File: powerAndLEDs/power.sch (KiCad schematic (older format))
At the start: 23 parts, among them J1 Conn_Coaxial_Power, J2 GS3, J3 Screw_Terminal_01x02, SW1 SW_SPST

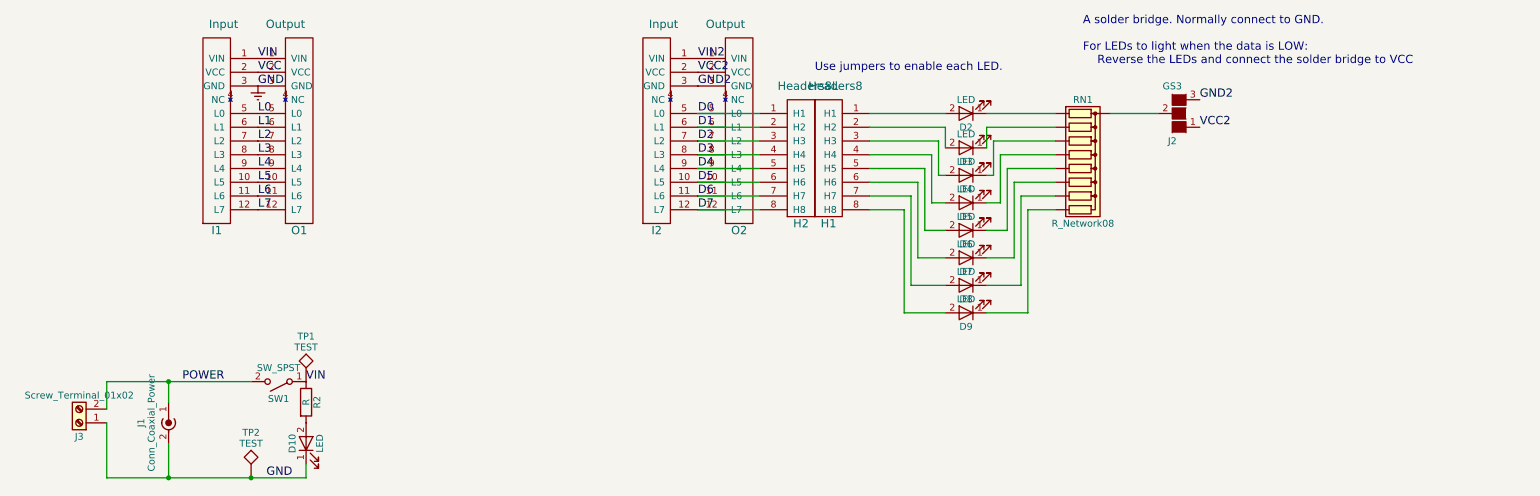
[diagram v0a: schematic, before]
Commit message: More update to make the libraryies use only relative paths.
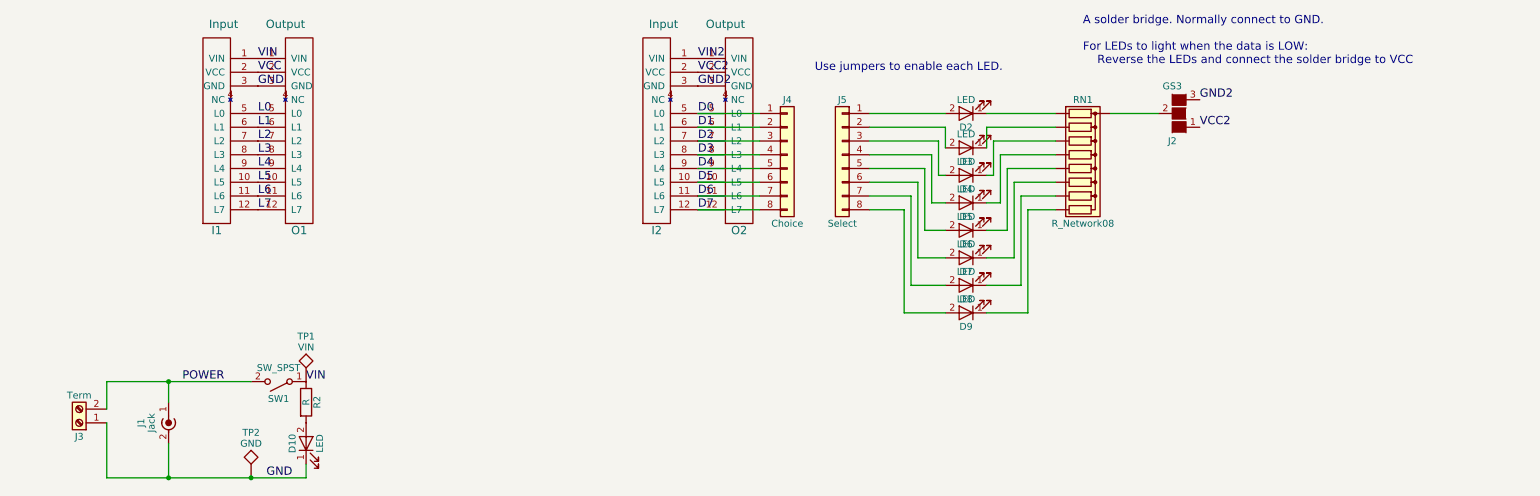
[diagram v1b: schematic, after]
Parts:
- removed H1: Headers8, Pin_Headers:Pin_Header_Straight_1x08_Pitch2.54mm, symbol Headers8
- removed H2: Headers8L, Pin_Headers:Pin_Header_Straight_1x08_Pitch2.54mm, symbol Headers8L
- added J4: Choice, Pin_Headers:Pin_Header_Straight_1x08_Pitch2.54mm, symbol Conn_01x08
- added J5: Select, Pin_Headers:Pin_Header_Straight_1x08_Pitch2.54mm, symbol Conn_01x08
- J1: value Conn_Coaxial_Power -> Jack
- J3: value Screw_Terminal_01x02 -> Term
- TP1: value TEST -> VIN
- TP2: value TEST -> GND
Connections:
- net D0: now also J4.1 (Pin_1)
- net D1: now also J4.2 (Pin_2)
- net D2: now also J4.3 (Pin_3)
- net D3: now also J4.4 (Pin_4)
- net D4: now also J4.5 (Pin_5)
- net D5: now also J4.6 (Pin_6)
- net D6: now also J4.7 (Pin_7)
- net D7: now also J4.8 (Pin_8)
- net at D2.2 (A): now also J5.1 (Pin_1)
- net at D3.2 (A): now also J5.2 (Pin_2)
- net at D4.2 (A): now also J5.3 (Pin_3)
- net at D5.2 (A): now also J5.4 (Pin_4)
- net at D6.2 (A): now also J5.5 (Pin_5)
- net at D7.2 (A): now also J5.6 (Pin_6)
- net at D8.2 (A): now also J5.7 (Pin_7)
- net at D9.2 (A): now also J5.8 (Pin_8)
- net Earth renamed GND
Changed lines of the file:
@@
 LIBS:valves
 LIBS:eplay
-LIBS:power-cache
 EELAYER 25 0
 EELAYER END
@@
 L7
 $Comp
-L Earth #PWR01
-U 1 1 5AC24527
-P 2400 1950
-F 0 "#PWR01" H 2400 1700 50  0001 C CNN
-F 1 "Earth" H 2400 1800 50  0001 C CNN
-F 2 "" H 2400 1950 50  0001 C CNN
-F 3 "" H 2400 1950 50  0001 C CNN
-	1    2400 1950
-	1    0    0    -1
-$EndComp
-$Comp
 L Input I1
 U 1 1 5AC3D559
@@
 P 1750 4350
 F 0 "J1" V 1550 4300 50  0000 C CNN
-F 1 "Conn_Coaxial_Power" V 1625 4300 50  0000 C CNN
+F 1 "Jack" V 1625 4300 50  0000 C CNN
 F 2 "Connectors:BARREL_JACK" H 1750 4300 50  0001 C CNN
 F 3 "" H 1750 4300 50  0001 C CNN
@@
 	1    7550 2150
 	-1   0    0    1
-$EndComp
-$Comp
-L Headers8 H1
-U 1 1 5AC3E37C
-P 6550 1900
-F 0 "H1" H 6550 850 60  0000 C CNN
-F 1 "Headers8" H 6600 1850 60  0000 C CNN
-F 2 "Pin_Headers:Pin_Header_Straight_1x08_Pitch2.54mm" H 6600 1850 60  0001 C CNN
-F 3 "" H 6600 1850 60  0001 C CNN
-	1    6550 1900
-	1    0    0    -1
 $EndComp
 $Comp
@@
 GND2
 $Comp
-L Headers8L H2
-U 1 1 5AC403D4
-P 6350 1900
-F 0 "H2" H 6350 850 60  0000 C CNN
-F 1 "Headers8L" H 6400 1850 60  0000 C CNN
-F 2 "Pin_Headers:Pin_Header_Straight_1x08_Pitch2.54mm" H 6400 1850 60  0001 C CNN
-F 3 "" H 6400 1850 60  0001 C CNN
-	1    6350 1900
-	1    0    0    -1
-$EndComp
-$Comp
 L R_Network08 RN1
 U 1 1 5AC40AE5
@@
 P 2750 4100
 F 0 "TP1" H 2750 4400 50  0000 C BNN
-F 1 "TEST" H 2750 4350 50  0000 C CNN
+F 1 "VIN" H 2750 4350 50  0000 C CNN
 F 2 "Connectors:PINTST" H 2750 4100 50  0001 C CNN
 F 3 "" H 2750 4100 50  0001 C CNN
@@
 P 2350 4800
 F 0 "TP2" H 2350 5100 50  0000 C BNN
-F 1 "TEST" H 2350 5050 50  0000 C CNN
+F 1 "GND" H 2350 5050 50  0000 C CNN
 F 2 "Connectors:PINTST" H 2350 4800 50  0001 C CNN
 F 3 "" H 2350 4800 50  0001 C CNN
@@
 P 1100 4400
 F 0 "J3" H 1100 4500 50  0000 C CNN
-F 1 "Screw_Terminal_01x02" H 1100 4200 50  0000 C CNN
+F 1 "Term" H 1100 4200 50  0000 C CNN
 F 2 "Connectors_Terminal_Blocks:TerminalBlock_Philmore_TB132_02x5mm_Straight" H 1100 4400 50  0001 C CNN
 F 3 "" H 1100 4400 50  0001 C CNN
@@
 	1300 4400 1300 4800
 Connection ~ 1750 4800
+$Comp
+L Conn_01x08 J4
+U 1 1 5AFEF822
+P 6250 2450
+F 0 "J4" H 6250 2850 50  0000 C CNN
+F 1 "Choice" H 6250 1950 50  0000 C CNN
+F 2 "Pin_Headers:Pin_Header_Straight_1x08_Pitch2.54mm" H 6250 2450 50  0001 C CNN
+F 3 "" H 6250 2450 50  0001 C CNN
+	1    6250 2450
+	1    0    0    -1
+$EndComp
+$Comp
+L Conn_01x08 J5
+U 1 1 5AFEF8FA
+P 6650 2450
+F 0 "J5" H 6650 2850 50  0000 C CNN
+F 1 "Select" H 6650 1950 50  0000 C CNN
+F 2 "Pin_Headers:Pin_Header_Straight_1x08_Pitch2.54mm" H 6650 2450 50  0001 C CNN
+F 3 "" H 6650 2450 50  0001 C CNN
+	1    6650 2450
+	-1   0    0    -1
+$EndComp
 $EndSCHEMATC
